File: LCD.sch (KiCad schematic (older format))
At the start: 7 parts, among them U1 RC1602A, U14 LM2776

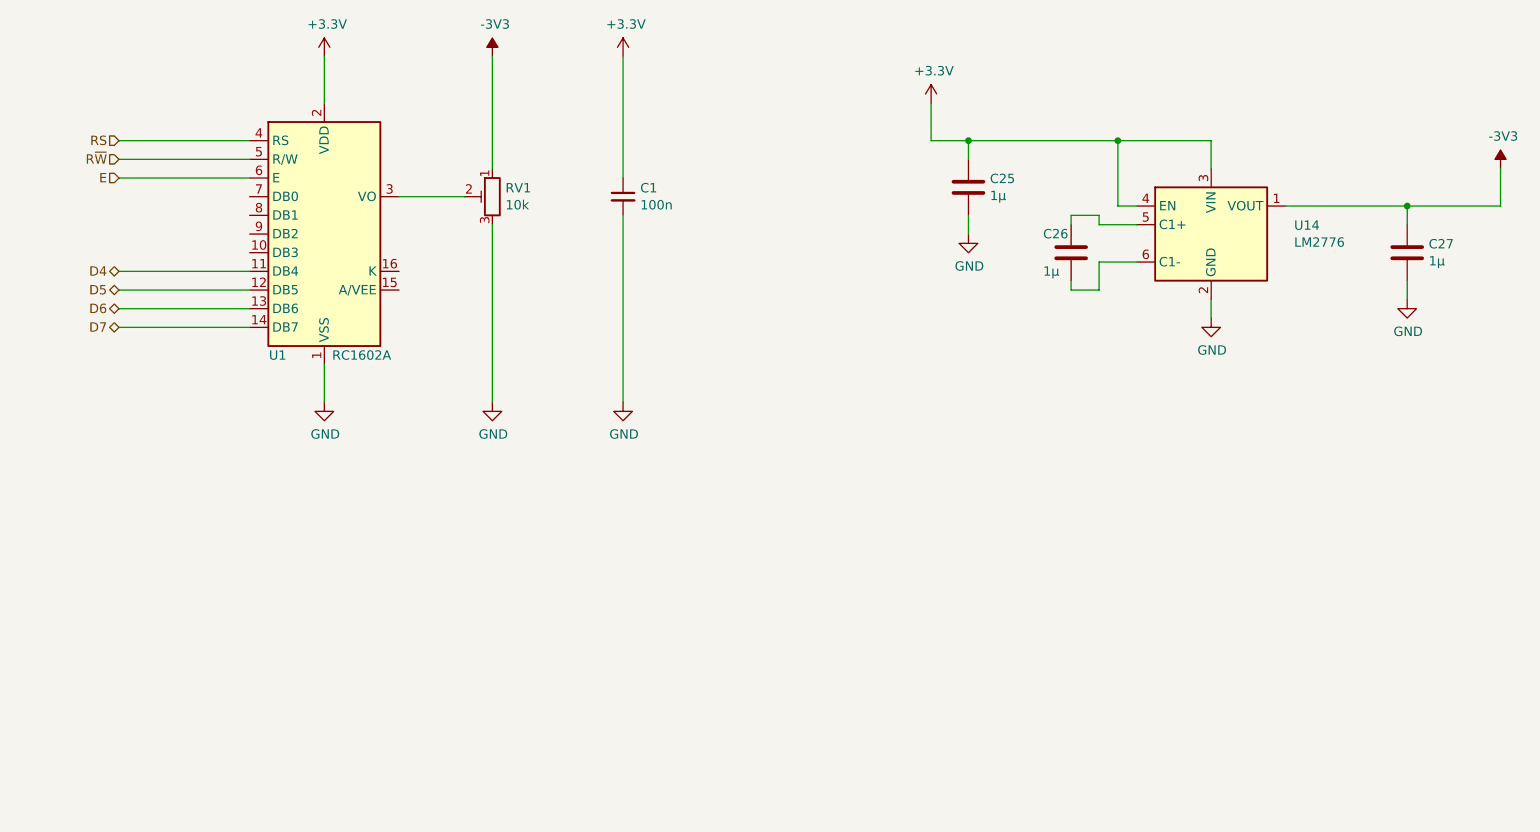
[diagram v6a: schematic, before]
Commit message: Alternative Footprints für Taster und LCD eingefügt
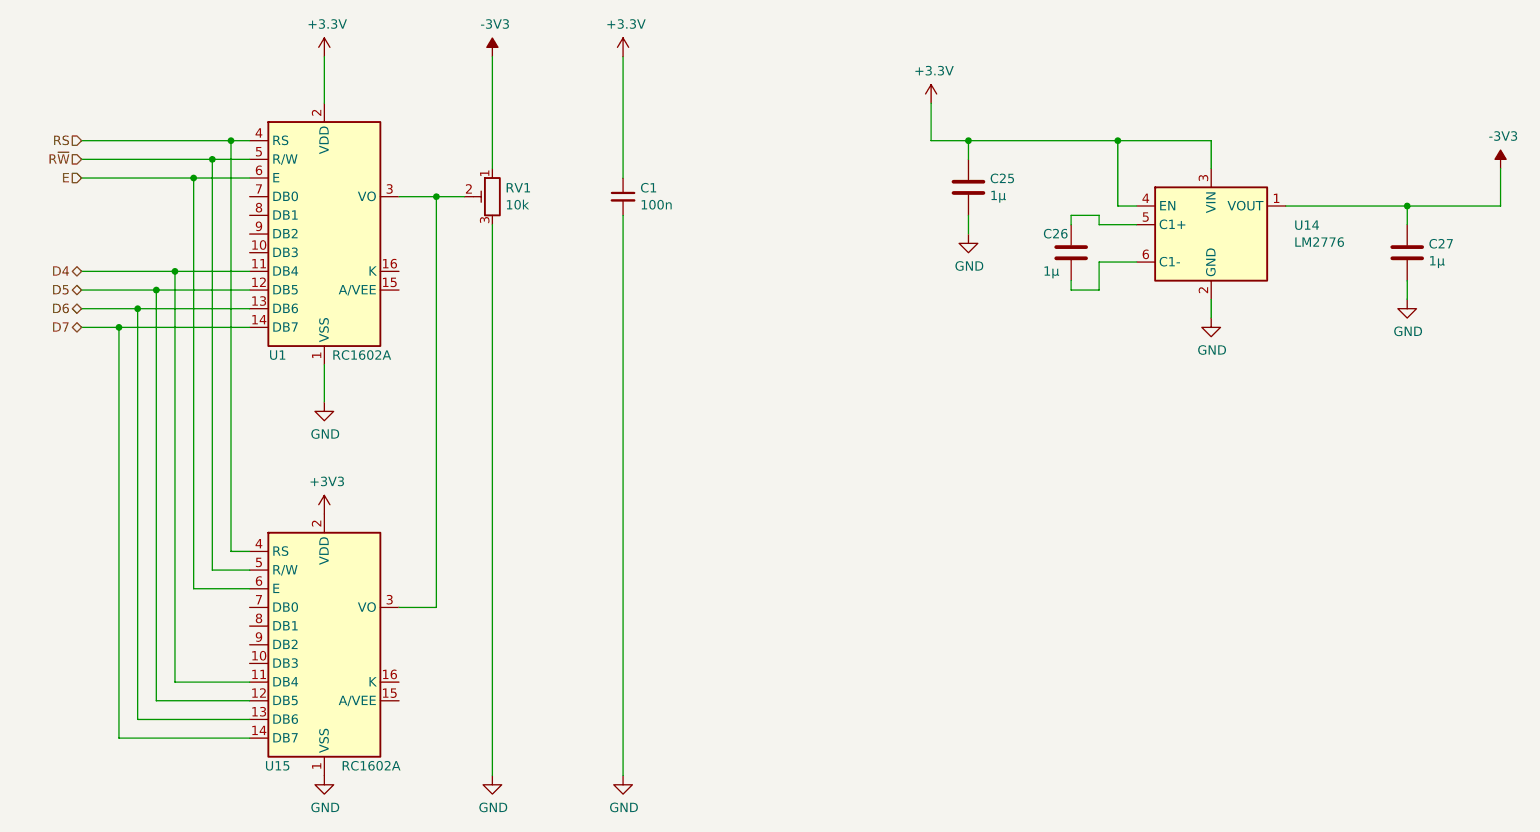
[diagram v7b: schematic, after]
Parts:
- added U15: RC1602A, Display:RC1602A, symbol Display_Character:RC1602A
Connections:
- net +3V3: now also U15.2 (VDD)
- net D4: now also U15.11 (DB4)
- net D5: now also U15.12 (DB5)
- net D6: now also U15.13 (DB6)
- net D7: now also U15.14 (DB7)
- net E: now also U15.6 (E)
- net GND: now also U15.1 (VSS)
- net RS: now also U15.4 (RS)
- net R~W~: now also U15.5 (R/W)
- net at RV1.2, U1.3 (VO): now also U15.3 (VO)
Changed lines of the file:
@@
 Comment4 ""
 $EndDescr
-Text HLabel 2100 3550 0    50   BiDi ~ 0
+Text HLabel 1900 3550 0    50   BiDi ~ 0
 D4
-Text HLabel 2100 3650 0    50   BiDi ~ 0
+Text HLabel 1900 3650 0    50   BiDi ~ 0
 D5
-Text HLabel 2100 3750 0    50   BiDi ~ 0
+Text HLabel 1900 3750 0    50   BiDi ~ 0
 D6
-Text HLabel 2100 3850 0    50   BiDi ~ 0
+Text HLabel 1900 3850 0    50   BiDi ~ 0
 D7
-Text HLabel 2100 2850 0    50   Input ~ 0
+Text HLabel 1900 2850 0    50   Input ~ 0
 RS
-Text HLabel 2100 2950 0    50   Input ~ 0
+Text HLabel 1900 2950 0    50   Input ~ 0
 R~W~
-Text HLabel 2100 3050 0    50   Input ~ 0
+Text HLabel 1900 3050 0    50   Input ~ 0
 E
 $Comp
@@
 $EndComp
 Wire Wire Line
-	3600 3150 3950 3150
+	3600 3150 3800 3150
 $Comp
 L MCT_Labor_5529-rescue:C_Small-Device C1
@@
 L MCT_Labor_5529-rescue:GND-power #PWR0106
 U 1 1 5EEFE087
-P 4100 4250
-F 0 "#PWR0106" H 4100 4000 50  0001 C CNN
-F 1 "GND" H 4105 4077 50  0000 C CNN
-F 2 "" H 4100 4250 50  0001 C CNN
-F 3 "" H 4100 4250 50  0001 C CNN
-	1    4100 4250
+P 4100 6250
+F 0 "#PWR0106" H 4100 6000 50  0001 C CNN
+F 1 "GND" H 4105 6077 50  0000 C CNN
+F 2 "" H 4100 6250 50  0001 C CNN
+F 3 "" H 4100 6250 50  0001 C CNN
+	1    4100 6250
 	1    0    0    -1
 $EndComp
@@
 L MCT_Labor_5529-rescue:GND-power #PWR0107
 U 1 1 5EEFE62A
-P 4800 4250
-F 0 "#PWR0107" H 4800 4000 50  0001 C CNN
-F 1 "GND" H 4805 4077 50  0000 C CNN
-F 2 "" H 4800 4250 50  0001 C CNN
-F 3 "" H 4800 4250 50  0001 C CNN
-	1    4800 4250
+P 4800 6250
+F 0 "#PWR0107" H 4800 6000 50  0001 C CNN
+F 1 "GND" H 4805 6077 50  0000 C CNN
+F 2 "" H 4800 6250 50  0001 C CNN
+F 3 "" H 4800 6250 50  0001 C CNN
+	1    4800 6250
 	1    0    0    -1
 $EndComp
@@
 	3200 4050 3200 4250
 Wire Wire Line
-	4100 4250 4100 3300
-Wire Wire Line
-	4800 3250 4800 4250
-Wire Wire Line
-	2100 2850 2800 2850
-Wire Wire Line
-	2100 2950 2800 2950
-Wire Wire Line
-	2100 3050 2800 3050
-Wire Wire Line
-	2100 3550 2800 3550
-Wire Wire Line
-	2100 3650 2800 3650
-Wire Wire Line
-	2100 3750 2800 3750
-Wire Wire Line
-	2100 3850 2800 3850
+	4100 6250 4100 3300
+Wire Wire Line
+	4800 3250 4800 6250
+Wire Wire Line
+	1900 3850 2100 3850
 $Comp
 L power:+3.3V #PWR07
@@
 	1    0    0    -1
 $EndComp
+$Comp
+L Display_Character:RC1602A U15
+U 1 1 608948E5
+P 3200 5550
+F 0 "U15" H 2950 4900 50  0000 C CNN
+F 1 "RC1602A" H 3450 4900 50  0000 C CNN
+F 2 "Display:RC1602A" H 3300 4750 50  0001 C CNN
+F 3 "http://www.raystar-optronics.com/down.php?ProID=18" H 3300 5450 50  0001 C CNN
+	1    3200 5550
+	1    0    0    -1
+$EndComp
+$Comp
+L power:GND #PWR0108
+U 1 1 60895641
+P 3200 6250
+F 0 "#PWR0108" H 3200 6000 50  0001 C CNN
+F 1 "GND" H 3205 6077 50  0000 C CNN
+F 2 "" H 3200 6250 50  0001 C CNN
+F 3 "" H 3200 6250 50  0001 C CNN
+	1    3200 6250
+	1    0    0    -1
+$EndComp
+$Comp
+L power:+3V3 #PWR0119
+U 1 1 60895C26
+P 3200 4850
+F 0 "#PWR0119" H 3200 4700 50  0001 C CNN
+F 1 "+3V3" H 3215 5023 50  0000 C CNN
+F 2 "" H 3200 4850 50  0001 C CNN
+F 3 "" H 3200 4850 50  0001 C CNN
+	1    3200 4850
+	1    0    0    -1
+$EndComp
+Wire Wire Line
+	2800 5050 2700 5050
+Wire Wire Line
+	2700 5050 2700 2850
+Wire Wire Line
+	2700 2850 2800 2850
+Wire Wire Line
+	2800 5150 2600 5150
+Wire Wire Line
+	2600 5150 2600 2950
+Wire Wire Line
+	2600 2950 2800 2950
+Wire Wire Line
+	2800 5250 2500 5250
+Wire Wire Line
+	2500 5250 2500 3050
+Wire Wire Line
+	2500 3050 2800 3050
+Wire Wire Line
+	2800 5750 2400 5750
+Wire Wire Line
+	2400 5750 2400 3550
+Wire Wire Line
+	2400 3550 2800 3550
+Wire Wire Line
+	2800 5850 2300 5850
+Wire Wire Line
+	2300 5850 2300 3650
+Wire Wire Line
+	2300 3650 2800 3650
+Wire Wire Line
+	2800 5950 2200 5950
+Wire Wire Line
+	2200 5950 2200 3750
+Wire Wire Line
+	2200 3750 2800 3750
+Wire Wire Line
+	1900 2850 2700 2850
+Connection ~ 2700 2850
+Wire Wire Line
+	1900 2950 2600 2950
+Connection ~ 2600 2950
+Wire Wire Line
+	1900 3050 2500 3050
+Connection ~ 2500 3050
+Wire Wire Line
+	1900 3550 2400 3550
+Connection ~ 2400 3550
+Wire Wire Line
+	1900 3650 2300 3650
+Connection ~ 2300 3650
+Wire Wire Line
+	1900 3750 2200 3750
+Connection ~ 2200 3750
+Wire Wire Line
+	2800 6050 2100 6050
+Wire Wire Line
+	2100 6050 2100 3850
+Connection ~ 2100 3850
+Wire Wire Line
+	2100 3850 2800 3850
+Wire Wire Line
+	3600 5350 3800 5350
+Wire Wire Line
+	3800 5350 3800 3150
+Connection ~ 3800 3150
+Wire Wire Line
+	3800 3150 3950 3150
 $EndSCHEMATC
